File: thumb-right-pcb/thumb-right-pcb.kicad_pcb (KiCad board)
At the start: 2 copper layers, 77 x 88 mm, 31 parts, among them J1 Conn_01x10

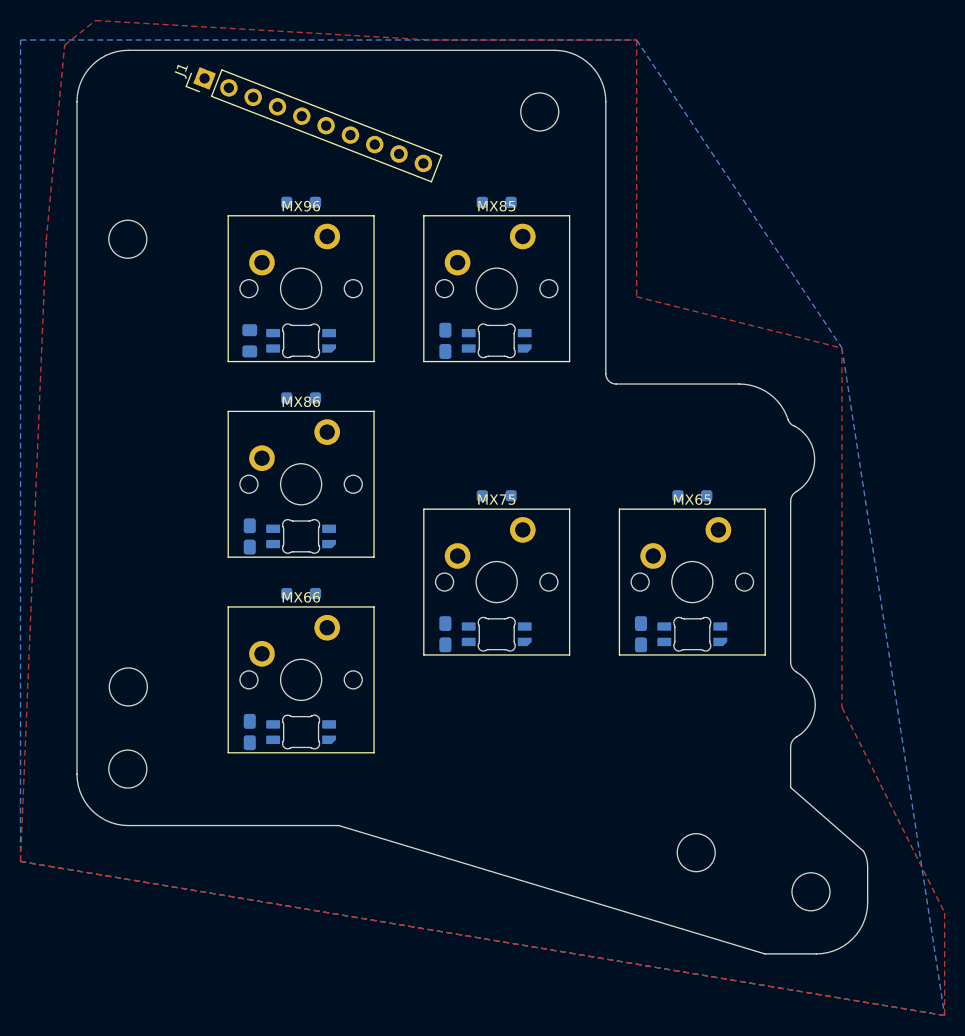
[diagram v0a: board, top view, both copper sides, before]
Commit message: Switch and diodes fully routed
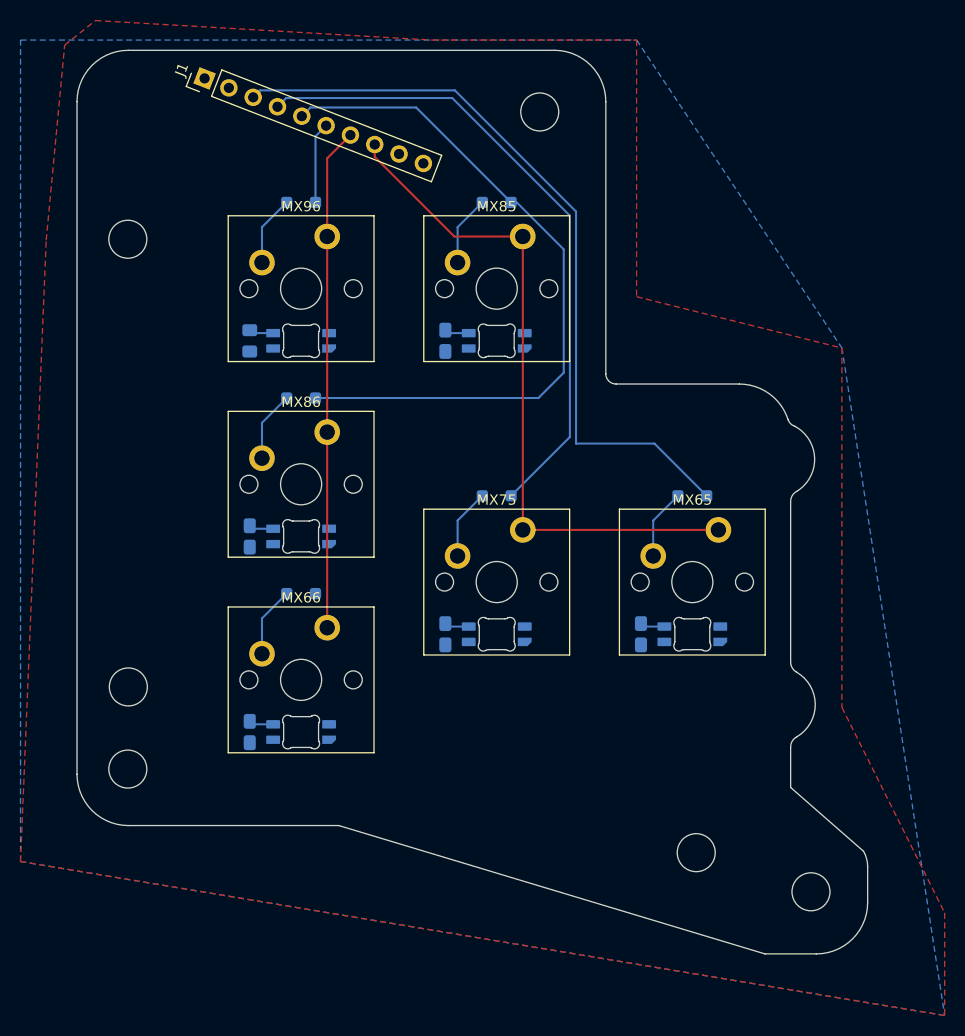
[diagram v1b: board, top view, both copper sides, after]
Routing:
- net /ROW_6: track 0.00 -> 74.0 mm
- net /ROW_8: track 0.00 -> 68.8 mm
- net /COL_R5: track 0.00 -> 66.5 mm
- net /ROW_7: track 0.00 -> 63.2 mm
- net /COL_R6: track 0.00 -> 48.9 mm
- net /VDD: track 0.00 -> 14.4 mm
- net /ROW_9: track 0.00 -> 7.90 mm
- net Net-(D96-A): track 0.00 -> 6.86 mm
- net Net-(D86-A): track 0.00 -> 6.86 mm
- net Net-(D66-A): track 0.00 -> 6.86 mm
- net Net-(D85-A): track 0.00 -> 6.86 mm
- net Net-(D75-A): track 0.00 -> 6.86 mm
- net Net-(D65-A): track 0.00 -> 6.86 mm

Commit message: Fully routed
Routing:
- net GND: track 0.00 -> 196.2 mm, vias 0 -> 6
- net /VDD: track 14.4 -> 193.6 mm, vias 0 -> 4
- net /ROW_6: track 74.0 -> 143.5 mm, vias 0 -> 2
- net Net-(LED65-DIN): track 0.00 -> 64.2 mm
- net /DOUT: track 0.00 -> 44.7 mm, vias 0 -> 1
- net Net-(LED75-DOUT): track 0.00 -> 42.8 mm, vias 0 -> 2
- net /DIN: track 0.00 -> 34.5 mm
- net Net-(LED86-DIN): track 0.00 -> 27.5 mm
- net Net-(LED66-DIN): track 0.00 -> 27.1 mm
- net Net-(LED65-DOUT): track 0.00 -> 16.0 mm
